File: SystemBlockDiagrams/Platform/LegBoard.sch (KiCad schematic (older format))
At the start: 16 parts

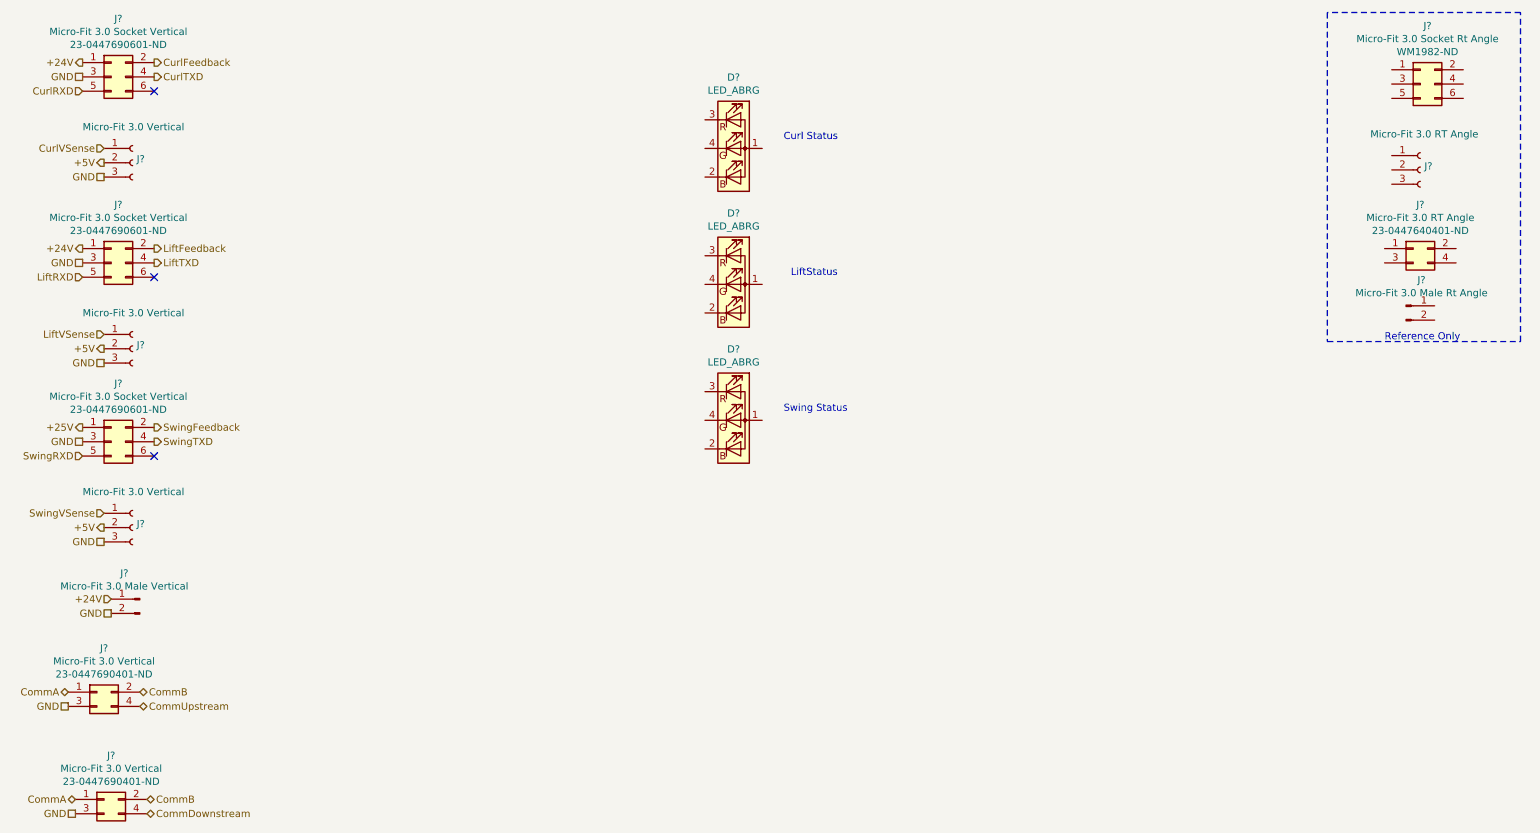
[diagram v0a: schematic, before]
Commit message: Connector updates
Change S2 cable to pre-made set
Add power connectors
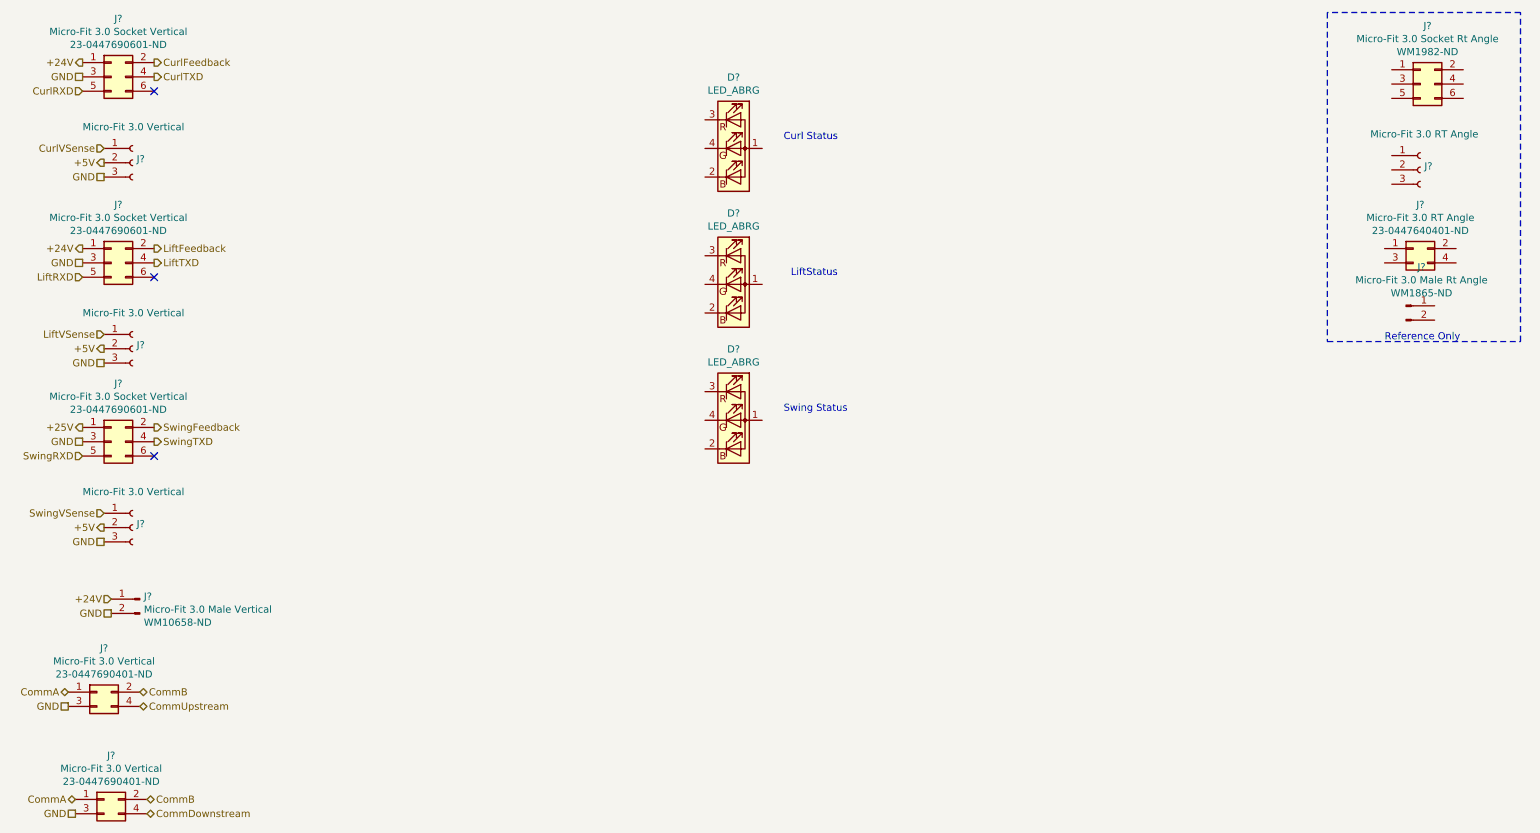
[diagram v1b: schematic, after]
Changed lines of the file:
@@
 U 1 1 5E238EBB
 P 1450 4650
-F 0 "J?" H 1558 4831 50  0000 C CNN
-F 1 "Micro-Fit 3.0 Male Vertical" H 1558 4740 50  0000 C CNN
+F 0 "J?" H 1422 4669 50  0000 R CNN
+F 1 "Micro-Fit 3.0 Male Vertical" H 1422 4578 50  0000 R CNN
 F 2 "" H 1450 4650 50  0001 C CNN
 F 3 "https://www.digikey.com/product-detail/en/molex/0436500228/WM10658-ND/3310542" H 1450 4650 50  0001 C CNN
@@
 F 5 "0436500228" H 1450 4650 50  0001 C CNN "Manufacturer Part Number"
 F 6 "Digi-Key" H 1450 4650 50  0001 C CNN "Supplier"
-F 7 "WM10658-ND" H 1450 4650 50  0001 C CNN "Supplier Part Number"
+F 7 "WM10658-ND" H 1422 4487 50  0000 R CNN "Supplier Part Number"
 	1    1450 4650
 	-1   0    0    -1
@@
 U 1 1 5E2390BD
 P 10300 2600
-F 0 "J?" H 10408 2781 50  0000 C CNN
-F 1 "Micro-Fit 3.0 Male Rt Angle" H 10408 2690 50  0000 C CNN
+F 0 "J?" H 10408 2871 50  0000 C CNN
+F 1 "Micro-Fit 3.0 Male Rt Angle" H 10408 2780 50  0000 C CNN
 F 2 "" H 10300 2600 50  0001 C CNN
 F 3 "https://www.digikey.com/product-detail/en/molex/0436500201/WM1865-ND/268994" H 10300 2600 50  0001 C CNN
@@
 F 5 "0436500201" H 10300 2600 50  0001 C CNN "Manufacturer Part Number"
 F 6 "Digi-Key" H 10300 2600 50  0001 C CNN "Supplier"
-F 7 "WM1865-ND" H 10300 2600 50  0001 C CNN "Supplier Part Number"
+F 7 "WM1865-ND" H 10408 2689 50  0000 C CNN "Supplier Part Number"
 	1    10300 2600
 	1    0    0    -1

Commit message: Switch Leg Board connectors
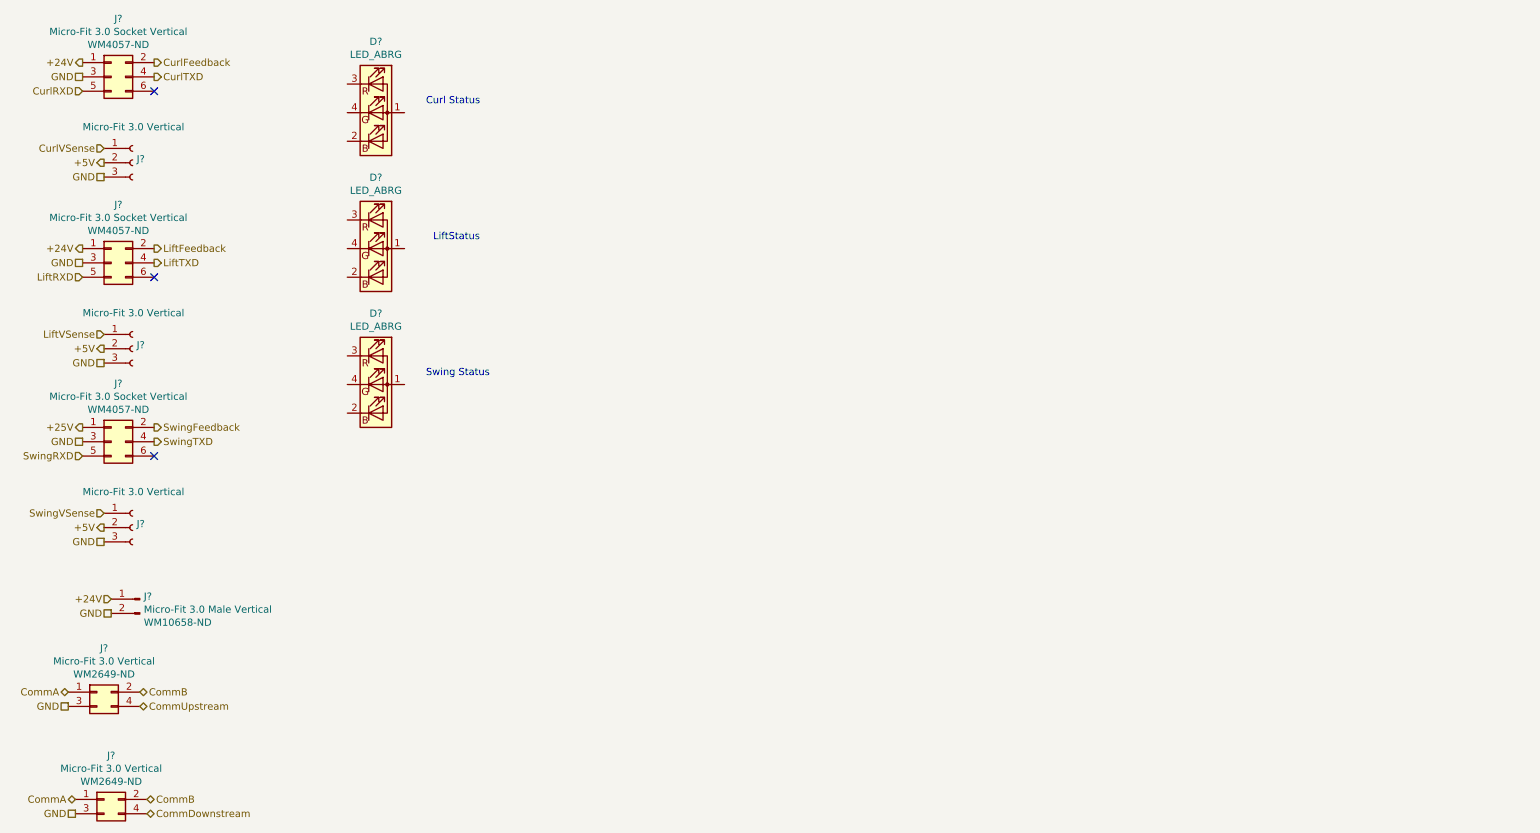
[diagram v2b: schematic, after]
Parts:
- removed J?: Micro-Fit 3.0 Socket Rt Angle, symbol Connector_Generic:Conn_02x03_Odd_Even
- removed J?: Micro-Fit 3.0 RT Angle, symbol Connector:Conn_01x03_Female
- removed J?: Micro-Fit 3.0 RT Angle, symbol Connector_Generic:Conn_02x02_Odd_Even
- removed J? (x2): Micro-Fit 3.0 Socket Vertical, symbol Connector_Generic:Conn_02x03_Odd_Even
- removed J?: Micro-Fit 3.0 Vertical, symbol Connector_Generic:Conn_02x02_Odd_Even
- removed J?: Micro-Fit 3.0 Male Rt Angle, symbol Connector:Conn_01x02_Male
- added J? (x2): Micro-Fit 3.0 Socket Vertical, symbol Connector_Generic:Conn_02x03_Odd_Even
- added J?: Micro-Fit 3.0 Vertical, symbol Connector_Generic:Conn_02x02_Odd_Even
- J?: Manufacturer (none) -> Molex; Manufacturer Part Number (none) -> 0430450625; Supplier Part Number 23-0447690601-ND -> WM4057-ND
- J?: Manufacturer Part Number 0447690401 -> 0430450413; Supplier DigiKey -> Digi-Key; Supplier Part Number 23-0447690401-ND -> WM2649-ND
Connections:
- net +24V: now also J?.1 (Pin_1)
- net +25V: now also J?.1 (Pin_1)
- net CommA: now also J?.1 (Pin_1)
- net CommB: now also J?.2 (Pin_2)
- net CommDownstream: now also J?.4 (Pin_4)
- net GND: now also J?.3 (Pin_3), J?.3 (Pin_3), J?.3 (Pin_3)
- net LiftFeedback: now also J?.2 (Pin_2)
- net LiftRXD: now also J?.5 (Pin_5)
- net LiftTXD: now also J?.4 (Pin_4)
- net SwingFeedback: now also J?.2 (Pin_2)
- net SwingRXD: now also J?.5 (Pin_5)
- net SwingTXD: now also J?.4 (Pin_4)
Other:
- note removed: "Reference Only"
- moved on the sheet: D?
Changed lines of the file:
@@
 F 1 "Micro-Fit 3.0 Socket Vertical" H 1300 1316 50  0000 C CNN
 F 2 "" H 1250 1000 50  0001 C CNN
-F 3 "https://www.digikey.com/product-detail/en/molex/0447690601/23-0447690601-ND/513217" H 1250 1000 50  0001 C CNN
+F 3 "https://www.digikey.com/products/en?keywords=WM4057-ND" H 1250 1000 50  0001 C CNN
 F 4 "Digi-Key" H 1250 1000 50  0001 C CNN "Supplier"
-F 5 " 23-0447690601-ND " H 1300 1225 50  0000 C CNN "Supplier Part Number"
+F 5 "WM4057-ND" H 1300 1225 50  0000 C CNN "Supplier Part Number"
+F 6 "Molex" H 1250 1000 50  0001 C CNN "Manufacturer"
+F 7 "0430450625" H 1250 1000 50  0001 C CNN "Manufacturer Part Number"
 	1    1250 1000
-	1    0    0    -1
-$EndComp
-$Comp
-L Connector:Conn_01x03_Female J?
-U 1 1 5E1D7826
-P 10400 1650
-F 0 "J?" H 10428 1676 50  0000 L CNN
-F 1 "Micro-Fit 3.0 RT Angle" H 10050 1900 50  0000 L CNN
-F 2 "" H 10400 1650 50  0001 C CNN
-F 3 "~" H 10400 1650 50  0001 C CNN
-F 4 "Mouser" H 10400 1650 50  0001 C CNN "Supplier"
-F 5 " 538-43650-0304 " H 10400 1650 50  0001 C CNN "Supplier Part Number"
-F 6 "Molex" H 10400 1650 50  0001 C CNN "Manufacturer"
-F 7 "43650-0304" H 10400 1650 50  0001 C CNN "Manufacturer part Number"
-	1    10400 1650
 	1    0    0    -1
 $EndComp
@@
 $Comp
 L Connector_Generic:Conn_02x02_Odd_Even J?
-U 1 1 5E1D783A
-P 10350 2200
-F 0 "J?" H 10400 2507 50  0000 C CNN
-F 1 "Micro-Fit 3.0 RT Angle" H 10400 2416 50  0000 C CNN
-F 2 "" H 10350 2200 50  0001 C CNN
-F 3 "https://www.digikey.com/product-detail/en/molex/0447640401/23-0447640401-ND/513244" H 10350 2200 50  0001 C CNN
-F 4 "DigiKey" H 10350 2200 50  0001 C CNN "Supplier"
-F 5 "23-0447640401-ND" H 10400 2325 50  0000 C CNN "Supplier Part Number"
-F 6 "Molex" H 10350 2200 50  0001 C CNN "Manufacturer"
-F 7 "0447640401" H 10350 2200 50  0001 C CNN "Manufacturer Part Number"
-	1    10350 2200
-	1    0    0    -1
-$EndComp
-$Comp
-L Connector_Generic:Conn_02x02_Odd_Even J?
 U 1 1 5E1D7844
 P 1150 5300
@@
 F 1 "Micro-Fit 3.0 Vertical" H 1200 5516 50  0000 C CNN
 F 2 "" H 1150 5300 50  0001 C CNN
-F 3 "https://www.digikey.com/product-detail/en/molex/0447690401/23-0447690401-ND/513216" H 1150 5300 50  0001 C CNN
-F 4 "DigiKey" H 1150 5300 50  0001 C CNN "Supplier"
-F 5 "23-0447690401-ND" H 1200 5425 50  0000 C CNN "Supplier Part Number"
+F 3 "https://www.digikey.com/products/en?keywords=WM2649-ND" H 1150 5300 50  0001 C CNN
+F 4 "Digi-Key" H 1150 5300 50  0001 C CNN "Supplier"
+F 5 "WM2649-ND" H 1200 5425 50  0000 C CNN "Supplier Part Number"
 F 6 "Molex" H 1150 5300 50  0001 C CNN "Manufacturer"
-F 7 " 0447690401" H 1150 5300 50  0001 C CNN "Manufacturer Part Number"
+F 7 "0430450413" H 1150 5300 50  0001 C CNN "Manufacturer Part Number"
 	1    1150 5300
-	1    0    0    -1
-$EndComp
-$Comp
-L Connector_Generic:Conn_02x03_Odd_Even J?
-U 1 1 5E1D781C
-P 10400 1050
-F 0 "J?" H 10450 1457 50  0000 C CNN
-F 1 "Micro-Fit 3.0 Socket Rt Angle" H 10450 1366 50  0000 C CNN
-F 2 "" H 10400 1050 50  0001 C CNN
-F 3 "https://www.digikey.com/product-detail/en/molex/0447690601/23-0447690601-ND/513217" H 10400 1050 50  0001 C CNN
-F 4 "Digi-Key" H 10400 1050 50  0001 C CNN "Supplier"
-F 5 " WM1982-ND " H 10450 1275 50  0000 C CNN "Supplier Part Number"
-	1    10400 1050
-	1    0    0    -1
-$EndComp
-Text Notes 10150 2850 0    50   ~ 0
-Reference Only
-Wire Notes Line
-	9750 550  9750 2850
-Wire Notes Line
-	9750 2850 11100 2850
-Wire Notes Line
-	11100 2850 11100 550
-Wire Notes Line
-	11100 550  9750 550
-$Comp
-L Connector_Generic:Conn_02x03_Odd_Even J?
-U 1 1 5E2310EE
-P 1250 2300
-F 0 "J?" H 1300 2707 50  0000 C CNN
-F 1 "Micro-Fit 3.0 Socket Vertical" H 1300 2616 50  0000 C CNN
-F 2 "" H 1250 2300 50  0001 C CNN
-F 3 "https://www.digikey.com/product-detail/en/molex/0447690601/23-0447690601-ND/513217" H 1250 2300 50  0001 C CNN
-F 4 "Digi-Key" H 1250 2300 50  0001 C CNN "Supplier"
-F 5 " 23-0447690601-ND " H 1300 2525 50  0000 C CNN "Supplier Part Number"
-	1    1250 2300
 	1    0    0    -1
 $EndComp
@@
 $EndComp
 $Comp
-L Connector_Generic:Conn_02x03_Odd_Even J?
-U 1 1 5E232D1B
-P 1250 3550
-F 0 "J?" H 1300 3957 50  0000 C CNN
-F 1 "Micro-Fit 3.0 Socket Vertical" H 1300 3866 50  0000 C CNN
-F 2 "" H 1250 3550 50  0001 C CNN
-F 3 "https://www.digikey.com/product-detail/en/molex/0447690601/23-0447690601-ND/513217" H 1250 3550 50  0001 C CNN
-F 4 "Digi-Key" H 1250 3550 50  0001 C CNN "Supplier"
-F 5 " 23-0447690601-ND " H 1300 3775 50  0000 C CNN "Supplier Part Number"
-	1    1250 3550
-	1    0    0    -1
-$EndComp
-$Comp
 L Connector:Conn_01x03_Female J?
 U 1 1 5E232D29
@@
 F 7 "43650-0319" H 1400 4150 50  0001 C CNN "Manufacturer part Number"
 	1    1400 4150
-	1    0    0    -1
-$EndComp
-$Comp
-L Connector_Generic:Conn_02x02_Odd_Even J?
-U 1 1 5E238235
-P 1200 6050
-F 0 "J?" H 1250 6357 50  0000 C CNN
-F 1 "Micro-Fit 3.0 Vertical" H 1250 6266 50  0000 C CNN
-F 2 "" H 1200 6050 50  0001 C CNN
-F 3 "https://www.digikey.com/product-detail/en/molex/0447690401/23-0447690401-ND/513216" H 1200 6050 50  0001 C CNN
-F 4 "DigiKey" H 1200 6050 50  0001 C CNN "Supplier"
-F 5 "23-0447690401-ND" H 1250 6175 50  0000 C CNN "Supplier Part Number"
-F 6 "Molex" H 1200 6050 50  0001 C CNN "Manufacturer"
-F 7 " 0447690401" H 1200 6050 50  0001 C CNN "Manufacturer Part Number"
-	1    1200 6050
 	1    0    0    -1
 $EndComp
@@
 	1    1450 4650
 	-1   0    0    -1
-$EndComp
-$Comp
-L Connector:Conn_01x02_Male J?
-U 1 1 5E2390BD
-P 10300 2600
-F 0 "J?" H 10408 2871 50  0000 C CNN
-F 1 "Micro-Fit 3.0 Male Rt Angle" H 10408 2780 50  0000 C CNN
-F 2 "" H 10300 2600 50  0001 C CNN
-F 3 "https://www.digikey.com/product-detail/en/molex/0436500201/WM1865-ND/268994" H 10300 2600 50  0001 C CNN
-F 4 "Molex" H 10300 2600 50  0001 C CNN "Manufacturer"
-F 5 "0436500201" H 10300 2600 50  0001 C CNN "Manufacturer Part Number"
-F 6 "Digi-Key" H 10300 2600 50  0001 C CNN "Supplier"
-F 7 "WM1865-ND" H 10408 2689 50  0000 C CNN "Supplier Part Number"
-	1    10300 2600
-	1    0    0    -1
 $EndComp
 Text HLabel 1550 1000 2    50   Output ~ 0
@@
 L Device:LED_ABRG D?
 U 1 1 5E245915
-P 5600 1500
-F 0 "D?" H 5600 1997 50  0000 C CNN
-F 1 "LED_ABRG" H 5600 1906 50  0000 C CNN
-F 2 "" H 5600 1500 50  0001 C CNN
-F 3 "~" H 5600 1500 50  0001 C CNN
-	1    5600 1500
+P 3100 1250
+F 0 "D?" H 3100 1747 50  0000 C CNN
+F 1 "LED_ABRG" H 3100 1656 50  0000 C CNN
+F 2 "" H 3100 1250 50  0001 C CNN
+F 3 "~" H 3100 1250 50  0001 C CNN
+	1    3100 1250
 	1    0    0    -1
 $EndComp
@@
 L Device:LED_ABRG D?
 U 1 1 5E246353
-P 5600 2450
-F 0 "D?" H 5600 2947 50  0000 C CNN
-F 1 "LED_ABRG" H 5600 2856 50  0000 C CNN
-F 2 "" H 5600 2450 50  0001 C CNN
-F 3 "~" H 5600 2450 50  0001 C CNN
-	1    5600 2450
+P 3100 2200
+F 0 "D?" H 3100 2697 50  0000 C CNN
+F 1 "LED_ABRG" H 3100 2606 50  0000 C CNN
+F 2 "" H 3100 2200 50  0001 C CNN
+F 3 "~" H 3100 2200 50  0001 C CNN
+	1    3100 2200
 	1    0    0    -1
 $EndComp
@@
 L Device:LED_ABRG D?
 U 1 1 5E246805
-P 5600 3400
-F 0 "D?" H 5600 3897 50  0000 C CNN
-F 1 "LED_ABRG" H 5600 3806 50  0000 C CNN
-F 2 "" H 5600 3400 50  0001 C CNN
-F 3 "~" H 5600 3400 50  0001 C CNN
-	1    5600 3400
-	1    0    0    -1
-$EndComp
-Text Notes 5950 1450 0    50   ~ 0
+P 3100 3150
+F 0 "D?" H 3100 3647 50  0000 C CNN
+F 1 "LED_ABRG" H 3100 3556 50  0000 C CNN
+F 2 "" H 3100 3150 50  0001 C CNN
+F 3 "~" H 3100 3150 50  0001 C CNN
+	1    3100 3150
+	1    0    0    -1
+$EndComp
+Text Notes 3450 1200 0    50   ~ 0
 Curl Status
-Text Notes 5950 3350 0    50   ~ 0
+Text Notes 3450 3100 0    50   ~ 0
 Swing Status
-Text Notes 6000 2400 0    50   ~ 0
+Text Notes 3500 2150 0    50   ~ 0
 LiftStatus
+$Comp
+L Connector_Generic:Conn_02x03_Odd_Even J?
+U 1 1 5E23B759
+P 1250 2300
+F 0 "J?" H 1300 2707 50  0000 C CNN
+F 1 "Micro-Fit 3.0 Socket Vertical" H 1300 2616 50  0000 C CNN
+F 2 "" H 1250 2300 50  0001 C CNN
+F 3 "https://www.digikey.com/products/en?keywords=WM4057-ND" H 1250 2300 50  0001 C CNN
+F 4 "Digi-Key" H 1250 2300 50  0001 C CNN "Supplier"
+F 5 "WM4057-ND" H 1300 2525 50  0000 C CNN "Supplier Part Number"
+F 6 "Molex" H 1250 2300 50  0001 C CNN "Manufacturer"
+F 7 "0430450625" H 1250 2300 50  0001 C CNN "Manufacturer Part Number"
+	1    1250 2300
+	1    0    0    -1
+$EndComp
+$Comp
+L Connector_Generic:Conn_02x03_Odd_Even J?
+U 1 1 5E23C88B
+P 1250 3550
+F 0 "J?" H 1300 3957 50  0000 C CNN
+F 1 "Micro-Fit 3.0 Socket Vertical" H 1300 3866 50  0000 C CNN
+F 2 "" H 1250 3550 50  0001 C CNN
+F 3 "https://www.digikey.com/products/en?keywords=WM4057-ND" H 1250 3550 50  0001 C CNN
+F 4 "Digi-Key" H 1250 3550 50  0001 C CNN "Supplier"
+F 5 "WM4057-ND" H 1300 3775 50  0000 C CNN "Supplier Part Number"
+F 6 "Molex" H 1250 3550 50  0001 C CNN "Manufacturer"
+F 7 "0430450625" H 1250 3550 50  0001 C CNN "Manufacturer Part Number"
+	1    1250 3550
+	1    0    0    -1
+$EndComp
+$Comp
+L Connector_Generic:Conn_02x02_Odd_Even J?
+U 1 1 5E2412AD
+P 1200 6050
+F 0 "J?" H 1250 6357 50  0000 C CNN
+F 1 "Micro-Fit 3.0 Vertical" H 1250 6266 50  0000 C CNN
+F 2 "" H 1200 6050 50  0001 C CNN
+F 3 "https://www.digikey.com/products/en?keywords=WM2649-ND" H 1200 6050 50  0001 C CNN
+F 4 "Digi-Key" H 1200 6050 50  0001 C CNN "Supplier"
+F 5 "WM2649-ND" H 1250 6175 50  0000 C CNN "Supplier Part Number"
+F 6 "Molex" H 1200 6050 50  0001 C CNN "Manufacturer"
+F 7 "0430450413" H 1200 6050 50  0001 C CNN "Manufacturer Part Number"
+	1    1200 6050
+	1    0    0    -1
+$EndComp
 $EndSCHEMATC
